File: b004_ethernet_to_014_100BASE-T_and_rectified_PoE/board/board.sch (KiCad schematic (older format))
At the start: 6 parts, among them J1 009_1000BASE-T_2x5, J2 011_GPIO_2x3, J3 PoE_2x2, U1 7499211121A

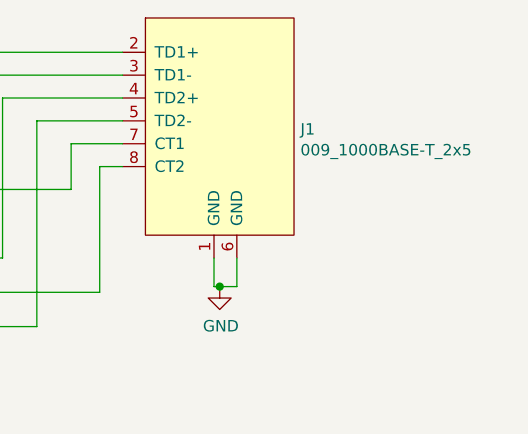
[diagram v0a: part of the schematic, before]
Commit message: updated folder name because the part supports 100base-t not 1000base-t
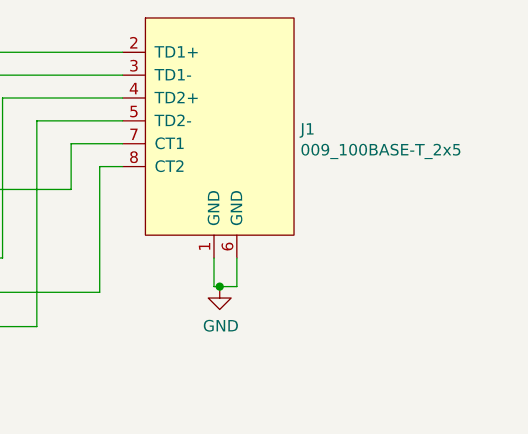
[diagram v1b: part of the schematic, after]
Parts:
- J1: value 009_1000BASE-T_2x5 -> 009_100BASE-T_2x5
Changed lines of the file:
@@
 P 4450 2650
 F 0 "J1" H 4778 2663 50  0000 L CNN
-F 1 "009_1000BASE-T_2x5" H 4778 2572 50  0000 L CNN
+F 1 "009_100BASE-T_2x5" H 4778 2572 50  0000 L CNN
 F 2 "on_edge:on_edge_2x05_device" H 4750 3300 50  0001 C CNN
 F 3 "" H 4750 3300 50  0001 C CNN

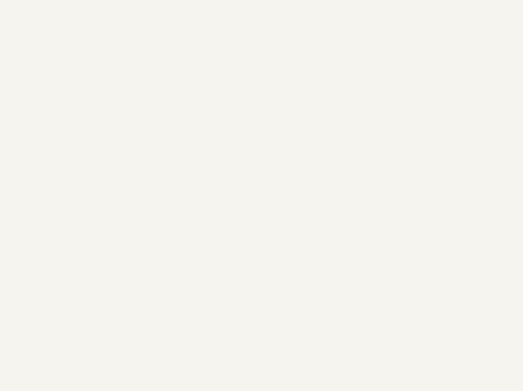
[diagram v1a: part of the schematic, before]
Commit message: added open hardware logo
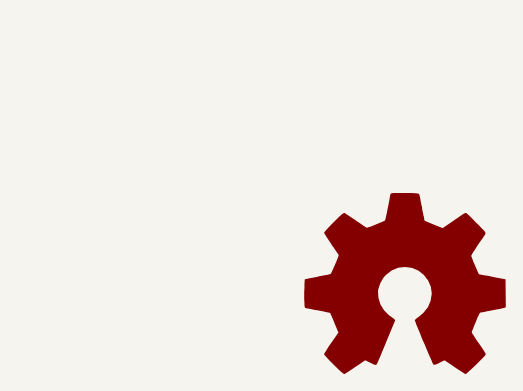
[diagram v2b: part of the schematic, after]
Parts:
- added l1: Logo_Open_Hardware_Large, Symbol:OSHW-Logo2_7.3x6mm_SilkScreen, symbol Graphic:Logo_Open_Hardware_Large
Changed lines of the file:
@@
 Wire Wire Line
 	2950 3350 3900 3350
+$Comp
+L Graphic:Logo_Open_Hardware_Large l1
+U 1 1 6111043A
+P 6925 5825
+F 0 "l1" H 6925 6325 50  0001 C CNN
+F 1 "Logo_Open_Hardware_Large" H 6925 5425 50  0001 C CNN
+F 2 "Symbol:OSHW-Logo2_7.3x6mm_SilkScreen" H 6925 5825 50  0001 C CNN
+F 3 "~" H 6925 5825 50  0001 C CNN
+	1    6925 5825
+	1    0    0    -1
+$EndComp
 $EndSCHEMATC
